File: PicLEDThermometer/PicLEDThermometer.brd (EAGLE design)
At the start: 60.6 x 58.4 mm, 13 parts, among them IC1 74LS595N, X1 1751248

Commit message: Add a voltage regulator.
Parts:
- added C1, C2: (no value), rcl:C025-030X050
- added Q1: MCP1702-3302E/TO, Microchip_By_element14_Batch_1:TO127P254X533-3
- moved X1 17.8 mm to (54.6, 10.2)
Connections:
- new net VDD: C1.1, Q1.2, X1.2
- net GNDA: now also C1.2, C2.2, Q1.1
- net VCC: now also C2.1, Q1.3; no longer X1.2
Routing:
- net VDD: track 0.00 -> 11.0 mm
- net VCC: track 67.3 -> 60.4 mm

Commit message: Change power input to padded holes.
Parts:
- removed X1: 1751248, con-phoenix-350:1751248
- added H1, H2: MOUNT-PAD-ROUND2.8, holes:2,8-PAD
- moved C1 6.35 mm to (55.9, 24.1)
- moved Q1 5.08 mm to (53.3, 27.9)
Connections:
- net GNDA: now also H2.B2,8; no longer X1.1
- net VDD: now also H1.B2,8; no longer X1.2
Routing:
- net VCC: track 60.4 -> 66.2 mm

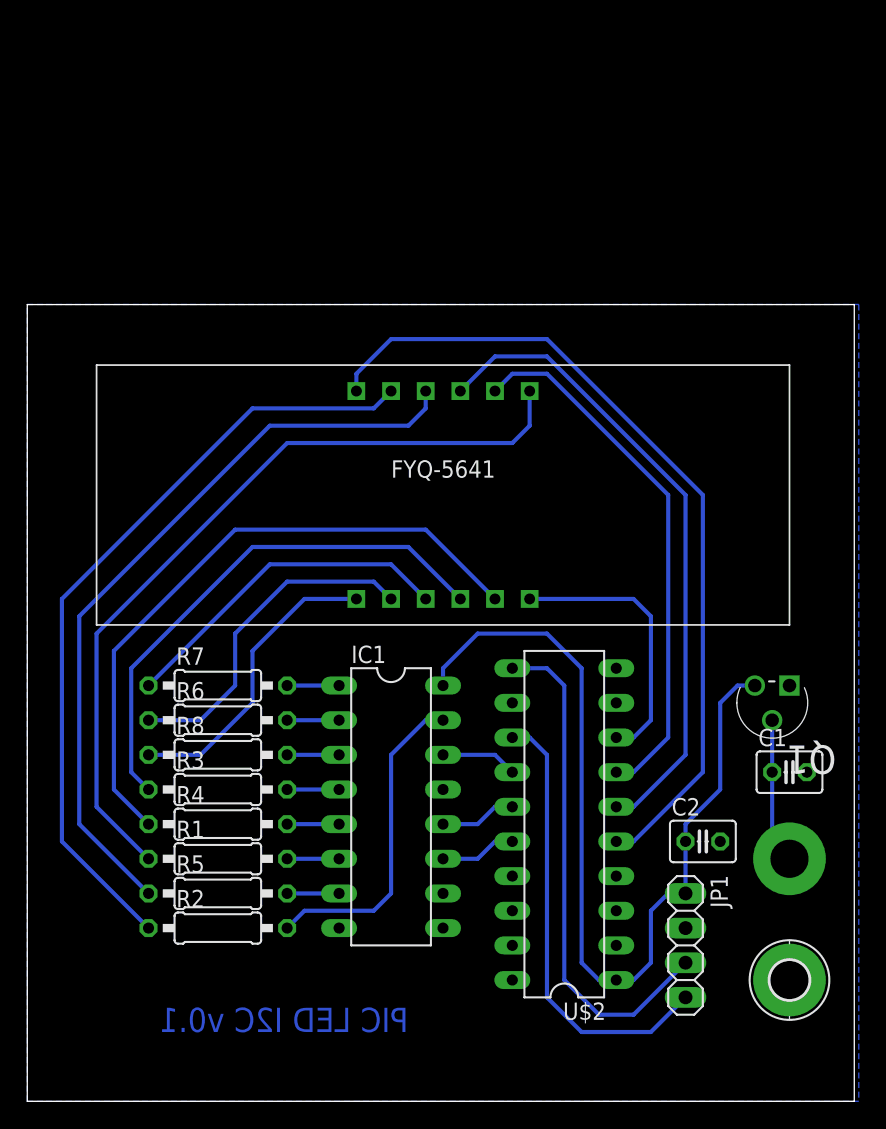
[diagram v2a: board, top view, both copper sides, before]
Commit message: Add a programming header. Moved I2C connector. Changed power connector to 2 pin header. Updated label to v0.2.
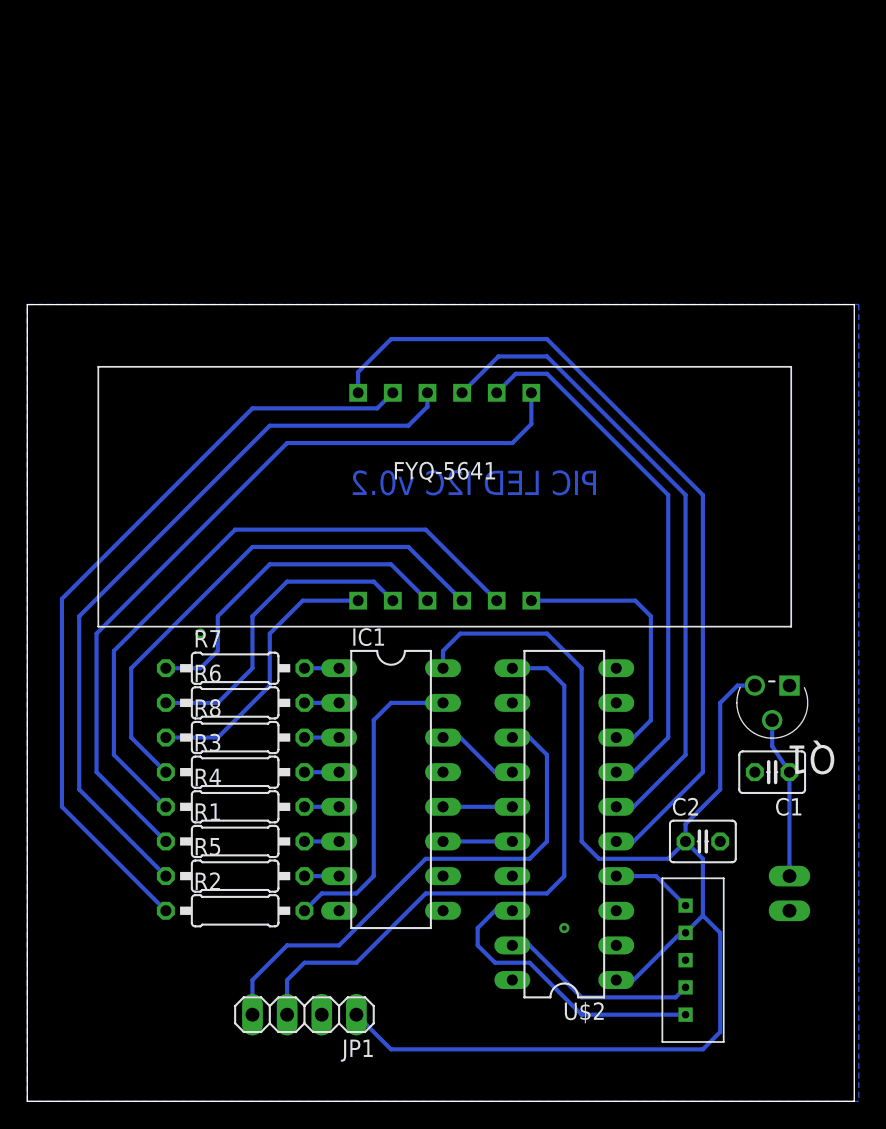
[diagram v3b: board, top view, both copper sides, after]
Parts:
- removed H2: MOUNT-PAD-ROUND2.8, holes:2,8-PAD
- added U$3: JST-PH-5POS, con-JST:JST-PH-5POS
- H1: device holes:2,8-PAD -> pinhead:1X02
- moved JP1 28.4 mm to (20.3, 6.35), turned to 180 degrees
- moved H1 2.54 mm to (55.9, 15.2), turned to 270 degrees
- moved R8 1.80 mm to (15.2, 26.7)
- moved R2 1.80 mm to (15.2, 14.0)
- moved R5 1.80 mm to (15.2, 16.5)
- moved R1 1.80 mm to (15.2, 19.1)
- moved R3 1.80 mm to (15.2, 24.1)
- moved R4 1.80 mm to (15.2, 21.6)
- moved R6 1.80 mm to (15.2, 29.2)
- moved R7 1.80 mm to (15.2, 31.8)
- moved C1 1.27 mm to (54.6, 24.1), turned to 180 degrees
- moved IC1 1.27 mm to (26.7, 22.9)
- moved U$1 0.18 mm to (30.6, 44.3)
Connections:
- new net N$10: U$2.RA1, U$3.P$5
- new net N$8: U$2.RA3, U$3.P$1
- new net N$9: U$2.RA0, U$3.P$4
- net GNDA: now also H1.2, U$3.P$3; no longer H2.B2,8
- net VCC: now also U$3.P$2
- net VDD: now also H1.1; no longer H1.B2,8
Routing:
- net VCC: track 66.2 -> 100.2 mm
- net N$10: track 0.00 -> 21.7 mm
- net N$9: track 0.00 -> 14.6 mm
- net SCL: track 37.4 -> 44.3 mm
- net N$8: track 0.00 -> 5.97 mm
- net SDA: track 33.1 -> 37.8 mm
- net N$12: track 22.2 -> 20.5 mm
- net N$4: track 24.7 -> 23.1 mm
- net LEDG: track 3.81 -> 2.54 mm
- net LEDF: track 3.81 -> 2.54 mm
- net LEDE: track 3.81 -> 2.54 mm
- net LEDDP: track 3.81 -> 2.54 mm
- net LEDD: track 3.81 -> 2.54 mm
- net LEDC: track 3.81 -> 2.54 mm
- net LEDB: track 3.81 -> 2.54 mm
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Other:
- board text added: "PIC LED I2C v0.2"
- board text removed: "PIC LED I2C v0.1"

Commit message: Add NPN transistors for LED cathodes. Add pull ups for I2C lines.
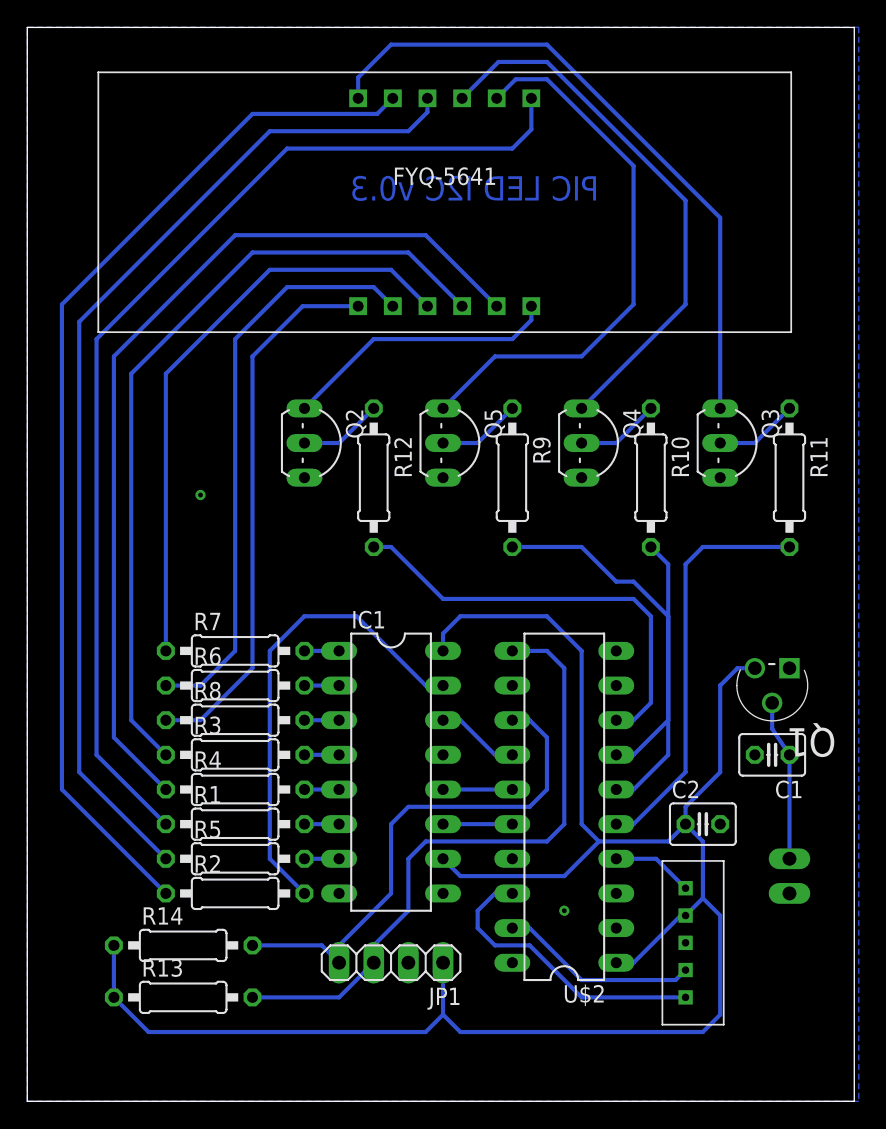
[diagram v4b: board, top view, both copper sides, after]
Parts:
- added Q2, Q3, Q4, Q5: 2N2222TO92, 2n2222:TO92-LINE
- added R10, R11, R12, R13, R14, R9: (no value), rcl:0207/10
- moved U$1 21.6 mm to (30.6, 65.9)
- moved JP1 7.41 mm to (26.7, 10.2)
- moved R7 1.27 mm to (15.2, 33.0)
- moved H1 1.27 mm to (55.9, 16.5)
- moved U$3 1.27 mm to (48.3, 12.6)
- moved C1 1.27 mm to (54.6, 25.4)
- moved C2 1.27 mm to (49.5, 20.3)
- moved IC1 1.27 mm to (26.7, 24.1)
- moved Q1 1.27 mm to (53.3, 29.2)
- moved R1 1.27 mm to (15.2, 20.3)
- moved R2 1.27 mm to (15.2, 15.2)
- moved R3 1.27 mm to (15.2, 25.4)
- moved R4 1.27 mm to (15.2, 22.9)
- moved R5 1.27 mm to (15.2, 17.8)
- moved R6 1.27 mm to (15.2, 30.5)
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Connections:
- removed net CLR: IC1.10
- new net N$11: R12.2, U$2.RC6
- new net N$13: R11.2, U$2.RC5
- new net N$14: R10.2, U$2.RC4
- new net N$15: R9.2, U$2.RC3
- new net N$16: Q2.BASE, R12.1
- new net N$17: Q3.BASE, R11.1
- new net N$18: Q4.BASE, R10.1
- new net N$19: Q5.BASE, R9.1
- net DIG1: now also Q3.COL; no longer U$2.RC5
- net DIG2: now also Q5.COL; no longer U$2.RC3
- net DIG3: now also Q2.COL; no longer U$2.RC6
- net DIG4: now also Q4.COL; no longer U$2.RC4
- net GNDA: now also IC1.13, Q2.EMIT, Q3.EMIT, Q4.EMIT, Q5.EMIT
- net SCL: now also R13.2
- net SDA: now also R14.2
- net VCC: now also IC1.10, R13.1, R14.1
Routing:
- net VCC: track 100.2 -> 139.7 mm
- net N$11: track 0.00 -> 31.8 mm
- net N$13: track 0.00 -> 30.0 mm
- net N$15: track 0.00 -> 26.0 mm
- net N$14: track 0.00 -> 20.6 mm
- net N$6: track 46.9 -> 67.2 mm
- net N$2: track 57.9 -> 78.2 mm
- net N$5: track 54.6 -> 74.9 mm
- net N$3: track 38.2 -> 58.6 mm
- net N$1: track 56.5 -> 76.9 mm
- net N$12: track 20.5 -> 40.1 mm
- net N$4: track 23.1 -> 42.7 mm
- net N$7: track 24.9 -> 43.8 mm
- net DIG1: track 61.3 -> 48.3 mm
- net LEDA: track 23.2 -> 34.7 mm
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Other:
- board size 60.6 x 58.4 mm -> 60.6 x 78.7 mm
- board text added: "PIC LED I2C v0.3"
- board text removed: "PIC LED I2C v0.2"

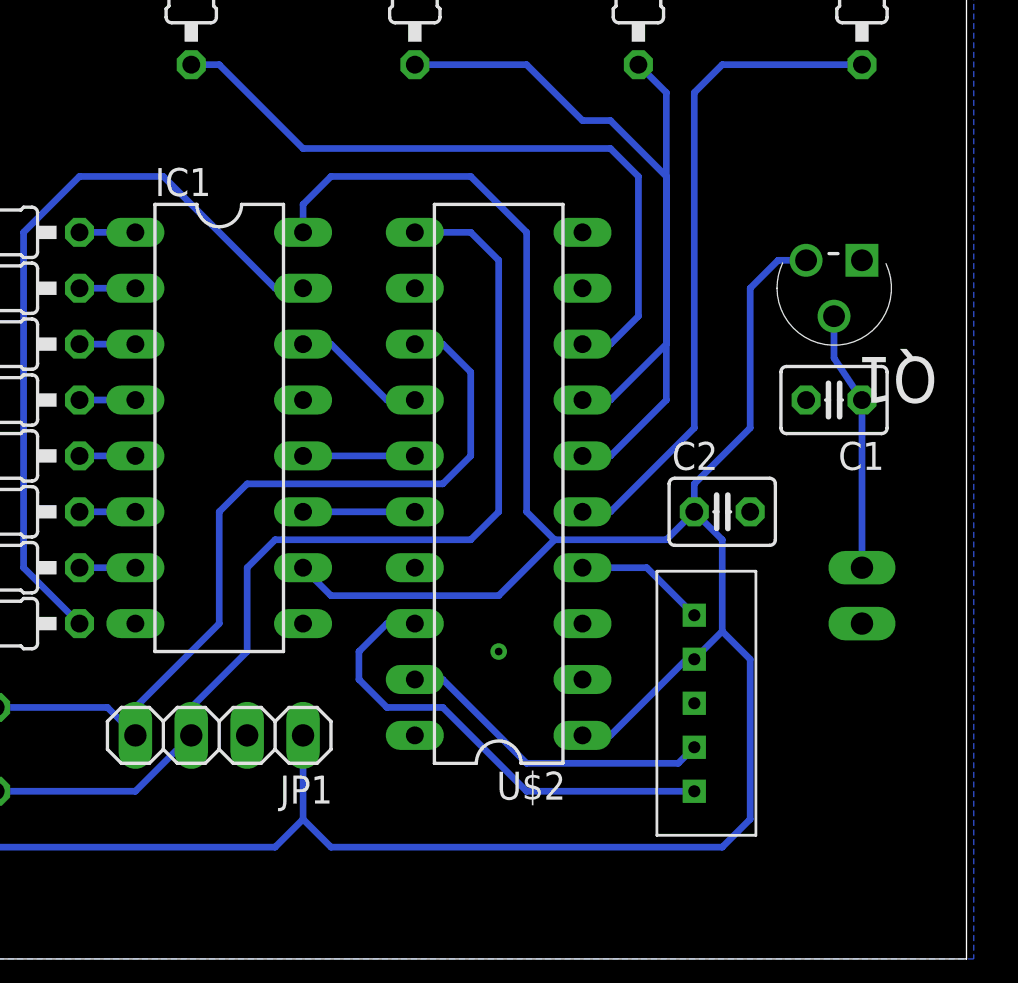
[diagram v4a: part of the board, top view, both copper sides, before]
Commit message: Change ICSP header to standard pin header. Add the ICSP resistor.
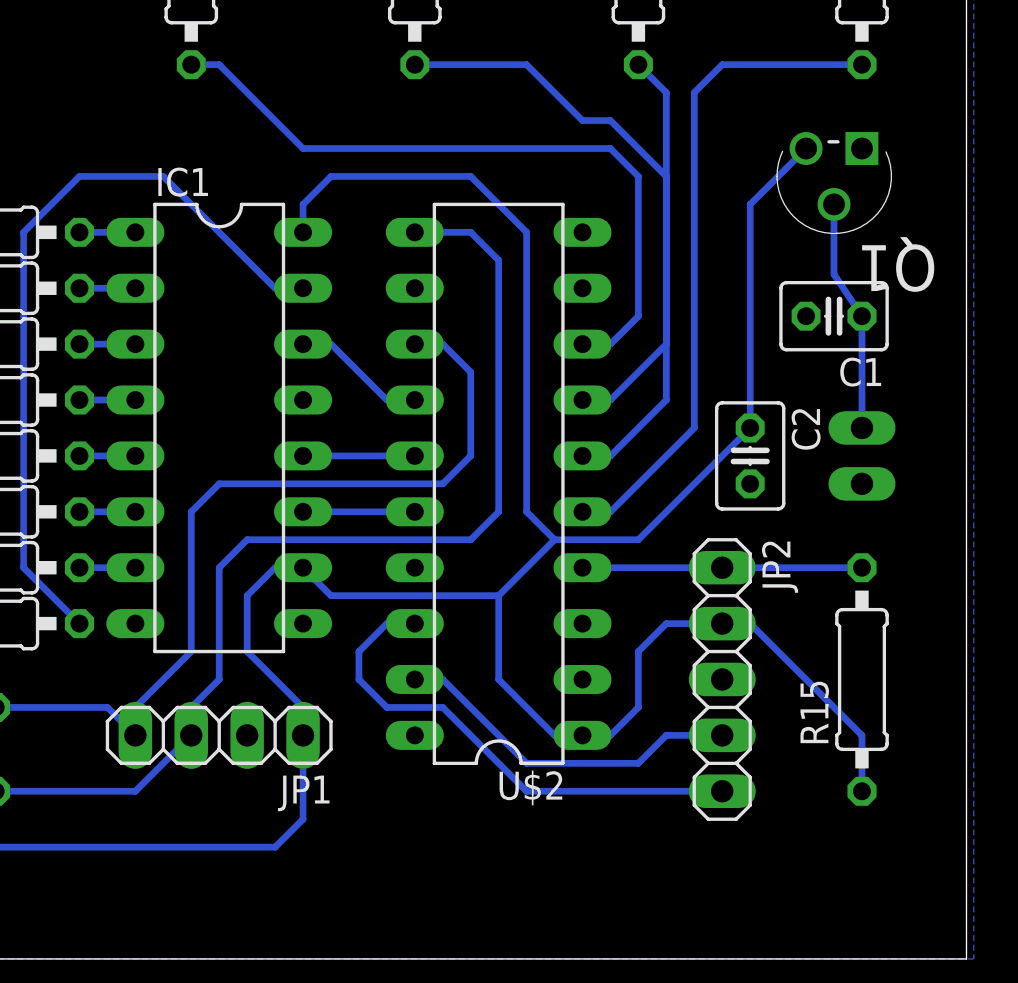
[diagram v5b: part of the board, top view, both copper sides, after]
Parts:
- removed U$3: JST-PH-5POS, con-JST:JST-PH-5POS
- added JP2: (no value), pinhead:1X05
- added R15: (no value), rcl:0207/10
- moved H1 6.35 mm to (55.9, 22.9)
- moved Q1 5.08 mm to (53.3, 34.3)
- moved C1 3.81 mm to (54.6, 29.2)
- moved C2 2.84 mm to (50.8, 22.9), turned to 270 degrees
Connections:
- net GNDA: now also JP2.3; no longer U$3.P$3
- net N$10: now also JP2.5; no longer U$3.P$5
- net N$8: now also JP2.1, R15.2; no longer U$3.P$1
- net N$9: now also JP2.4; no longer U$3.P$4
- net VCC: now also JP2.2, R15.1; no longer U$3.P$2
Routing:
- net N$8: track 5.97 -> 12.7 mm
- net N$9: track 14.6 -> 16.1 mm
- net N$10: track 21.7 -> 23.0 mm
- net VDD: track 11.8 -> 10.5 mm
- net VCC: track 139.7 -> 138.7 mm
- net SCL: track 46.9 -> 47.6 mm
- net SDA: track 38.0 -> 38.7 mm

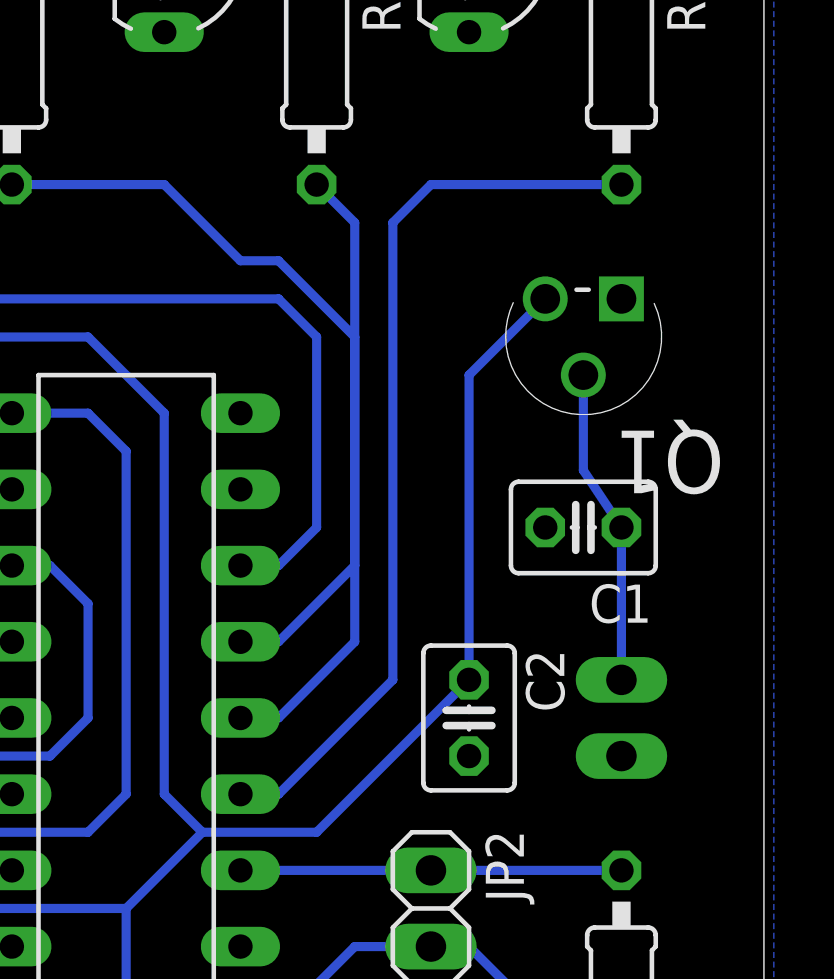
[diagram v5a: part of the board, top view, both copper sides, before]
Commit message: Fixed an overlapping trace.
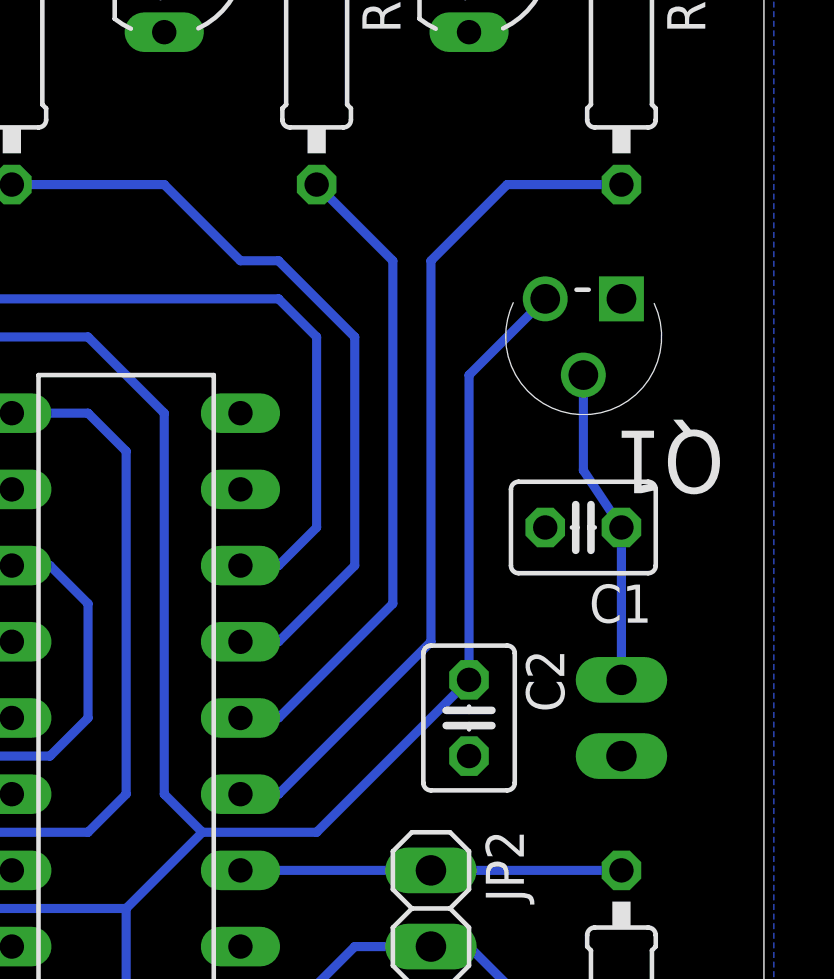
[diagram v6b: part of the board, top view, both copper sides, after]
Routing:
- net N$13: track 30.0 -> 28.6 mm
- net N$14: track 20.6 -> 21.7 mm
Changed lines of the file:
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@@
 <contactref element="U$2" pad="RC5"/>
 <wire x1="43.18" y1="20.32" x2="44.45" y2="20.32" width="0.3048" layer="16"/>
-<wire x1="44.45" y1="20.32" x2="48.26" y2="24.13" width="0.3048" layer="16"/>
-<wire x1="48.26" y1="24.13" x2="48.26" y2="39.37" width="0.3048" layer="16"/>
-<wire x1="48.26" y1="39.37" x2="49.53" y2="40.64" width="0.3048" layer="16"/>
-<wire x1="49.53" y1="40.64" x2="55.88" y2="40.64" width="0.3048" layer="16"/>
+<wire x1="44.45" y1="20.32" x2="49.53" y2="25.4" width="0.3048" layer="16"/>
+<wire x1="49.53" y1="25.4" x2="49.53" y2="38.1" width="0.3048" layer="16"/>
+<wire x1="49.53" y1="38.1" x2="52.07" y2="40.64" width="0.3048" layer="16"/>
+<wire x1="52.07" y1="40.64" x2="55.88" y2="40.64" width="0.3048" layer="16"/>
 </signal>
 <signal name="N$14">
@@
 <contactref element="U$2" pad="RC4"/>
 <wire x1="43.18" y1="22.86" x2="44.45" y2="22.86" width="0.3048" layer="16"/>
-<wire x1="44.45" y1="22.86" x2="46.99" y2="25.4" width="0.3048" layer="16"/>
-<wire x1="46.99" y1="25.4" x2="46.99" y2="39.37" width="0.3048" layer="16"/>
-<wire x1="46.99" y1="39.37" x2="45.72" y2="40.64" width="0.3048" layer="16"/>
+<wire x1="44.45" y1="22.86" x2="48.26" y2="26.67" width="0.3048" layer="16"/>
+<wire x1="48.26" y1="26.67" x2="48.26" y2="38.1" width="0.3048" layer="16"/>
+<wire x1="48.26" y1="38.1" x2="45.72" y2="40.64" width="0.3048" layer="16"/>
 </signal>
 <signal name="N$15">
